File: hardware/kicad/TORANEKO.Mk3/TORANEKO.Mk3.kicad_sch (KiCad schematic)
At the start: 84 parts, among them IC1 MP6551GQB-P, IC2 MP6551GQB-P, IC3 NCR321PASX, IC4 NCR321PASX, IC5 AS5047P-ATSM, IC6 STM32F411CEU6TR, IC7 AS5047P-ATSM, IC8 NCR321PASX, IC9 NCR321PASX, J1 Conn_01x02_Pin, J2 Conn_01x02_Pin, J3 Conn_01x02_Male, J4 Conn_01x02_Pin, J5 Conn_01x02_Pin, J6 Conn_02x03_Odd_Even, J7 Conn_01x02_Pin, Q1 IRLML6402, Q5 IRLML6344, SW1 SW_Push, U1 LSM6DSRXTR, U2 LXDC55FAAA-203, U3 Encord, U4 Encord_B, U5 Encord, U6 Encord_B, Y1 CSTNE10M0G52Z000R0

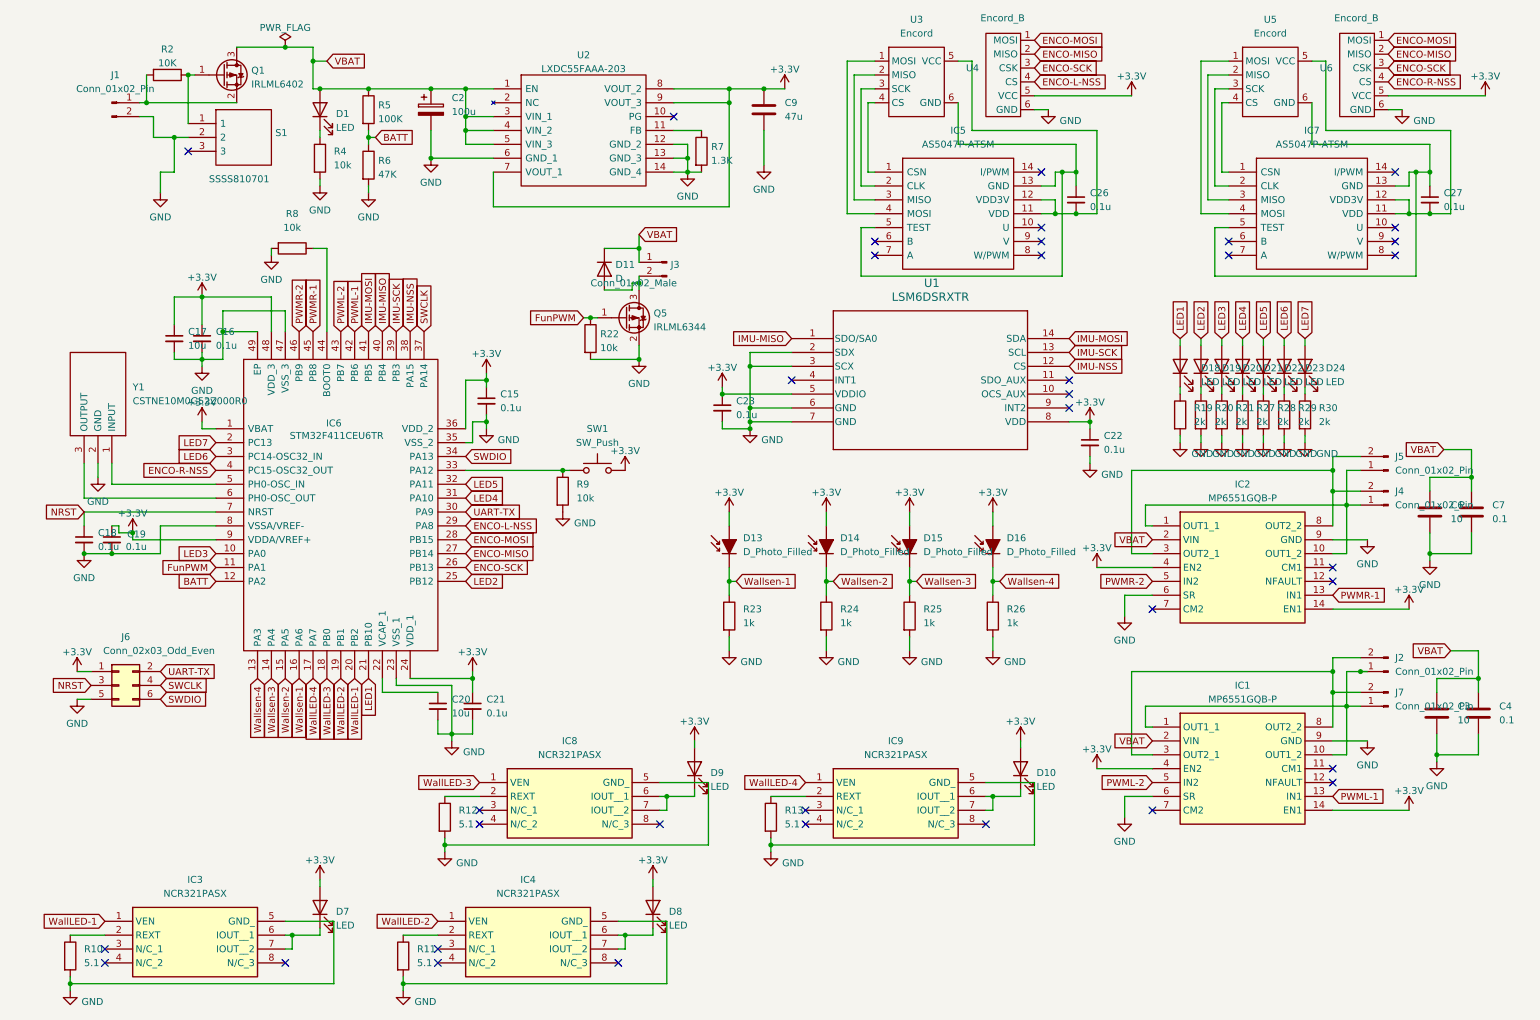
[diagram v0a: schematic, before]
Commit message: Update TORANEKO.Mk3 schematic
- Remove LED/resistor pairs D23/R29, D24/R30 and connectors J4, J7
- Add decoupling capacitor C24 (0.1u)
- Re-export schematic PDF

Co-Authored-By: Claude Opus 5.5 <noreply@anthropic.com>
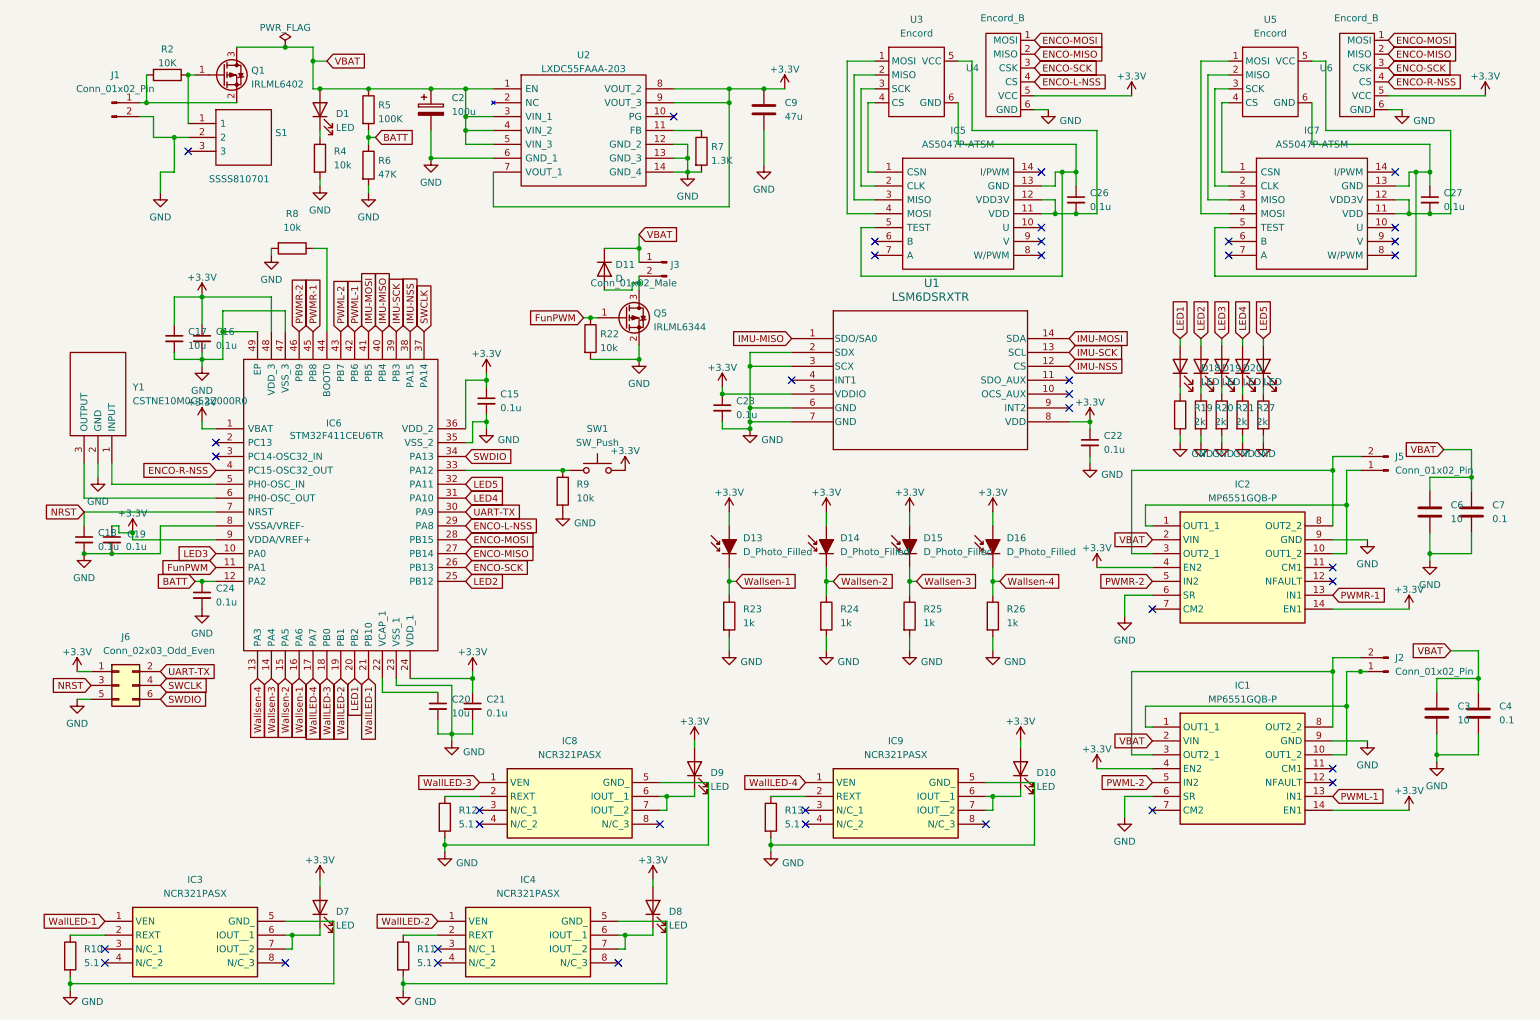
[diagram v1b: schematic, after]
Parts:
- removed D23, D24: LED, LED_SMD:LED_0402_1005Metric, symbol Device:LED
- removed J4, J7: Conn_01x02_Pin, Capacitor_SMD:C_0805_2012Metric, symbol Connector:Conn_01x02_Pin
- removed R29, R30: 2k, Resistor_SMD:R_0402_1005Metric, symbol Device:R
- added C24: 0.1u, Capacitor_SMD:C_0402_1005Metric, symbol Device:C_Small
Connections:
- net BATT: now also C24.1
- net GND: now also C24.2
- net LED1: now also IC6.20 (PB2); no longer IC6.21 (PB10)
- net WallLED-1: now also IC6.21 (PB10); no longer IC6.20 (PB2)
- net LED6: no longer names the net of IC6.3 (PC14-OSC32_IN)
- net LED7: no longer names the net of IC6.2 (PC13)
- no-connect marks 36 -> 38

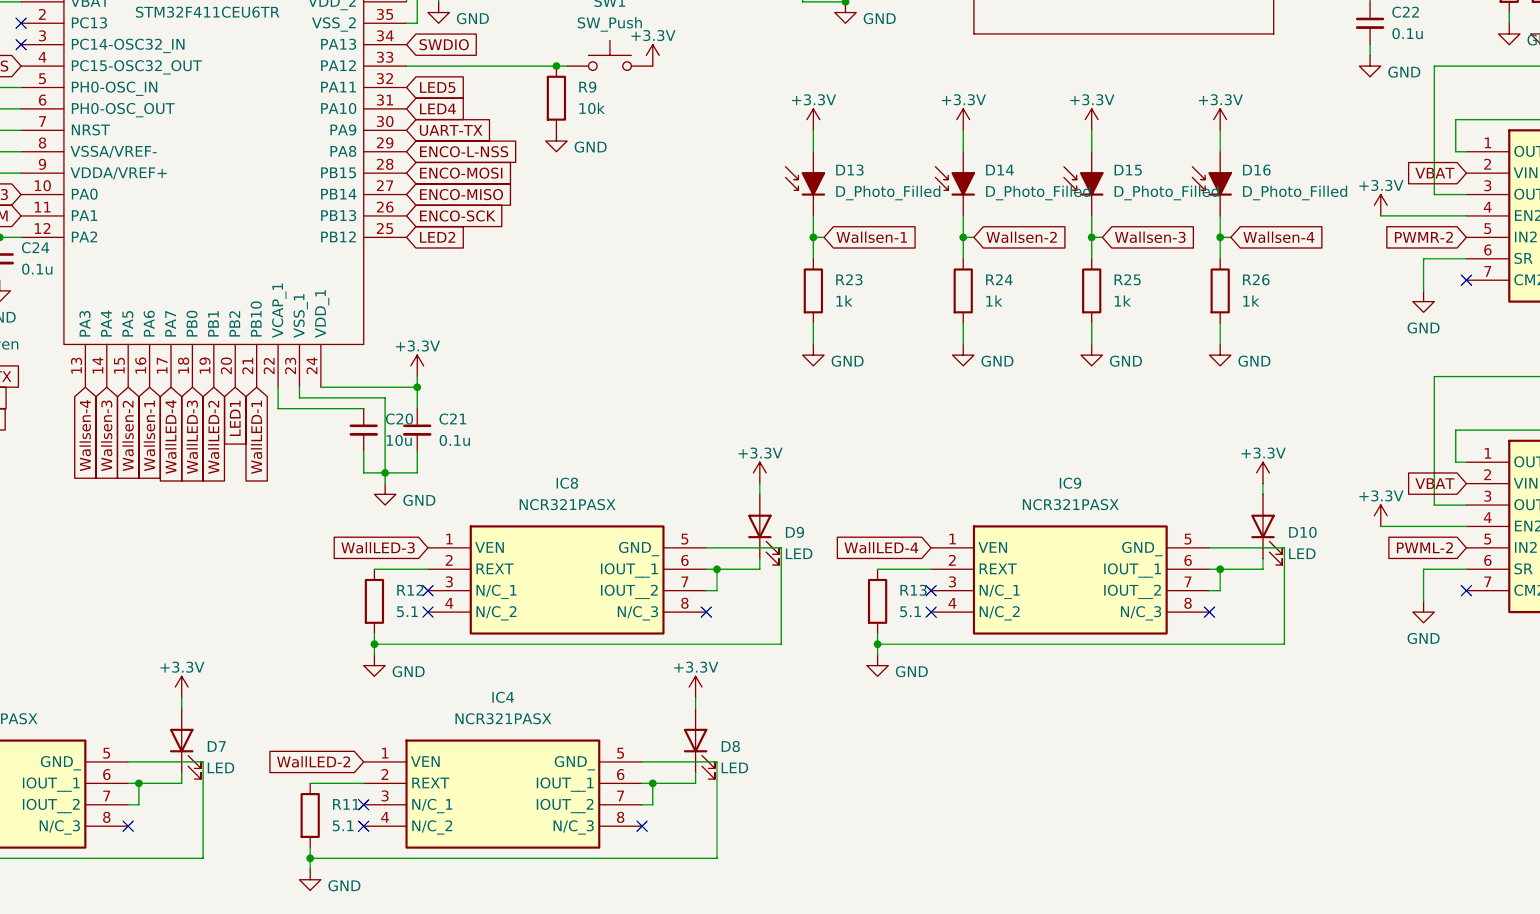
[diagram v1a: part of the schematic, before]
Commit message: Add decoupling capacitors C25, C28-C30 to TORANEKO.Mk3 schematic
- Add four 0.1u decoupling capacitors (C25, C28, C29, C30)
- Re-export schematic PDF

Co-Authored-By: Claude Opus 5.5 <noreply@anthropic.com>
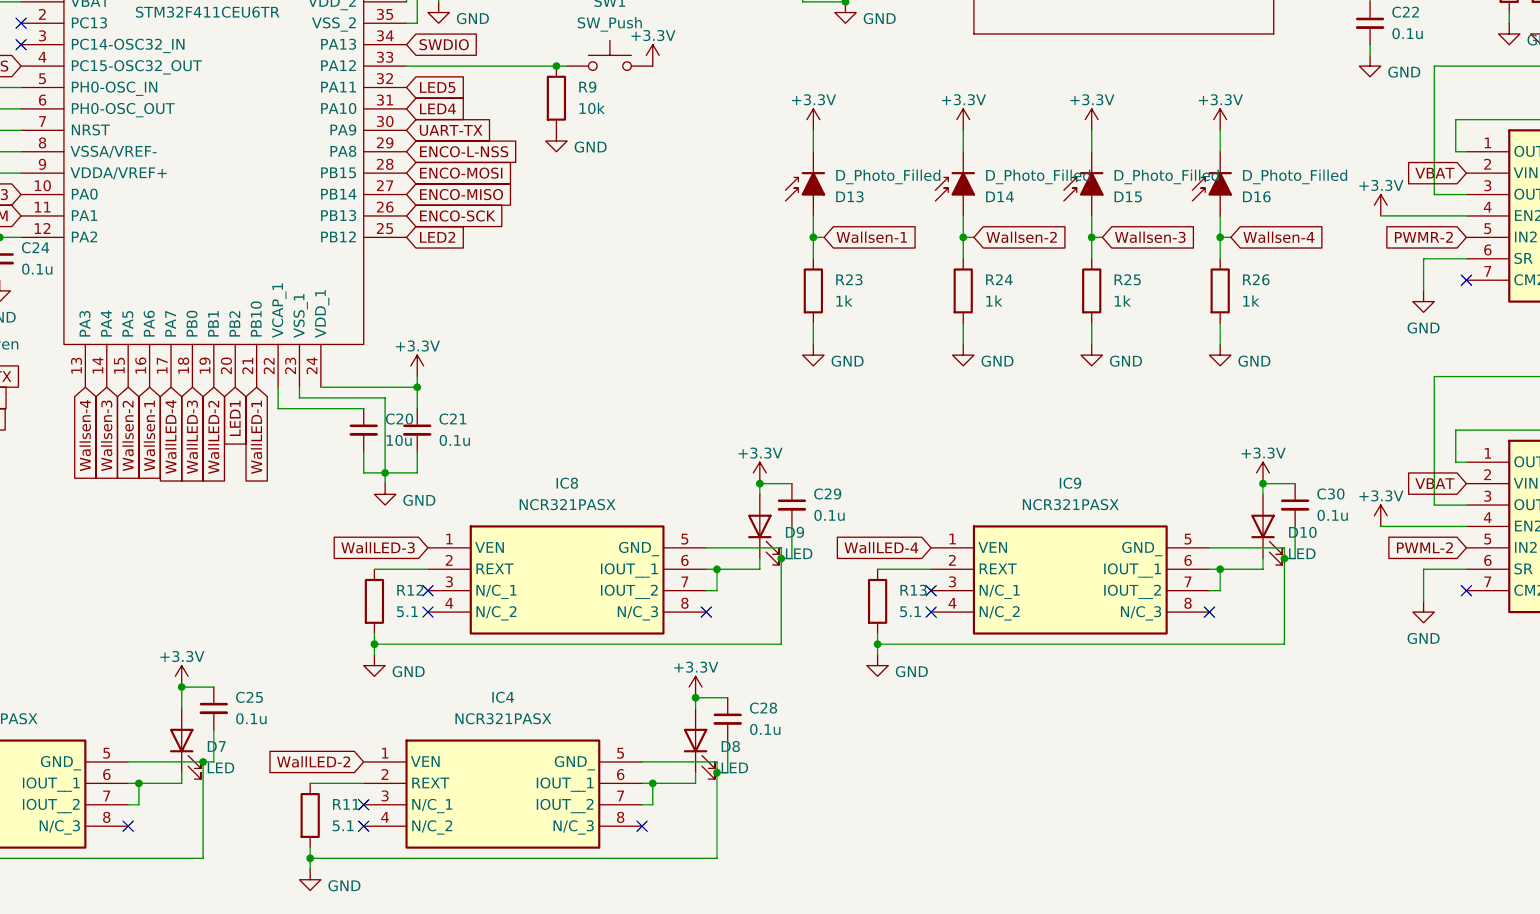
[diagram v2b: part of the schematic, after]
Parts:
- added C25, C28, C29, C30: 0.1u, Capacitor_SMD:C_0402_1005Metric, symbol Device:C_Small
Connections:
- net +3.3V: now also D13.1 (K), D14.1 (K), D15.1 (K), D16.1 (K), C25.1, C28.1, C29.1, C30.1; no longer D13.2 (A), D14.2 (A), D15.2 (A), D16.2 (A)
- net GND: now also C25.2, C28.2, C29.2, C30.2
- net Wallsen-1: now also D13.2 (A); no longer D13.1 (K)
- net Wallsen-2: now also D14.2 (A); no longer D14.1 (K)
- net Wallsen-3: now also D15.2 (A); no longer D15.1 (K)
- net Wallsen-4: now also D16.2 (A); no longer D16.1 (K)

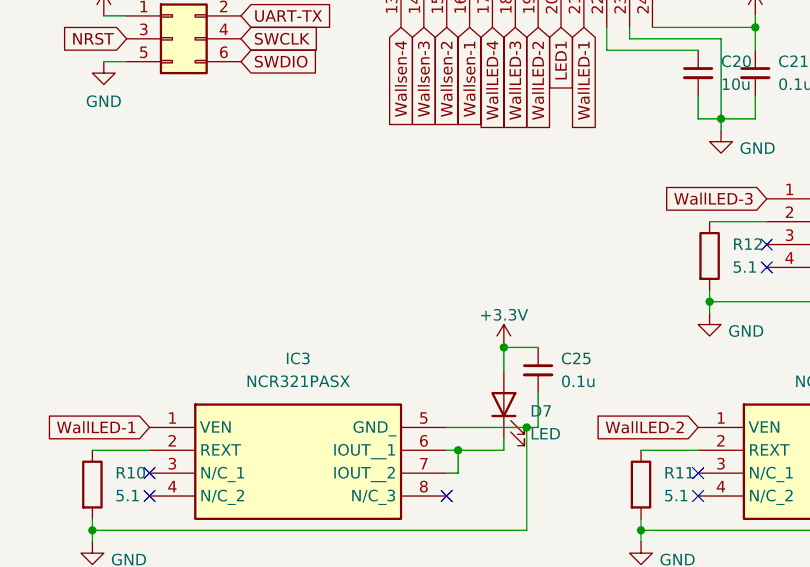
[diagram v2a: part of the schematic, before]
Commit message: Add 47u bulk capacitors C10, C11 on +3.3V to TORANEKO.Mk3 schematic
- Add two 47u capacitors (C10, C11) between +3.3V and GND
- Re-export schematic PDF

Co-Authored-By: Claude Opus 5.5 <noreply@anthropic.com>
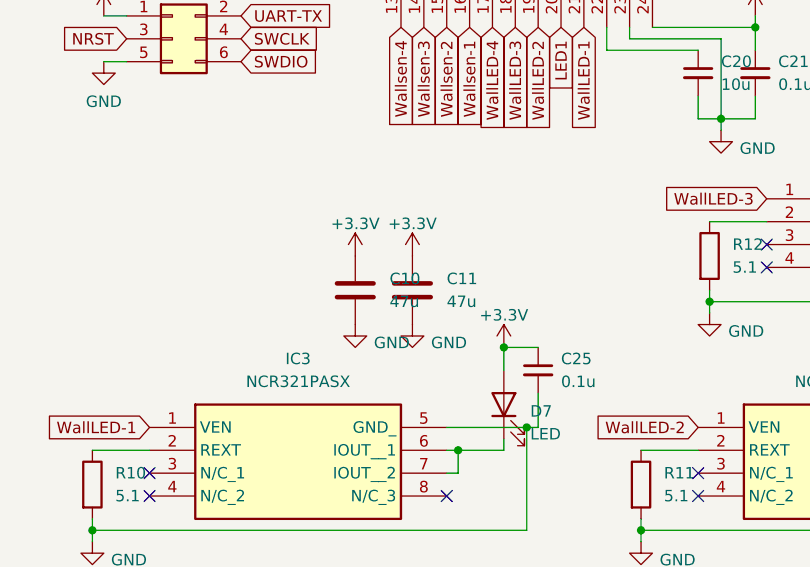
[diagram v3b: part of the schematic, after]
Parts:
- added C10, C11: 47u, Capacitor_SMD:C_0603_1608Metric, symbol Device:C
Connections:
- net +3.3V: now also C10.1, C11.1
- net GND: now also C10.2, C11.2
